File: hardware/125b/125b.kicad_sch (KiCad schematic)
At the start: 49 parts, among them J1 Guitar in, J2 Barrel_Jack, J3 Conn_02x05_Odd_Even_MountingP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, J4 Guitar out, SW1 SW_DIP_x02, SW2 RotaryEncoder_Switch, SW3 Switch 1, SW4 Switch 2, U1 L78L05_TO92, U2 TL074

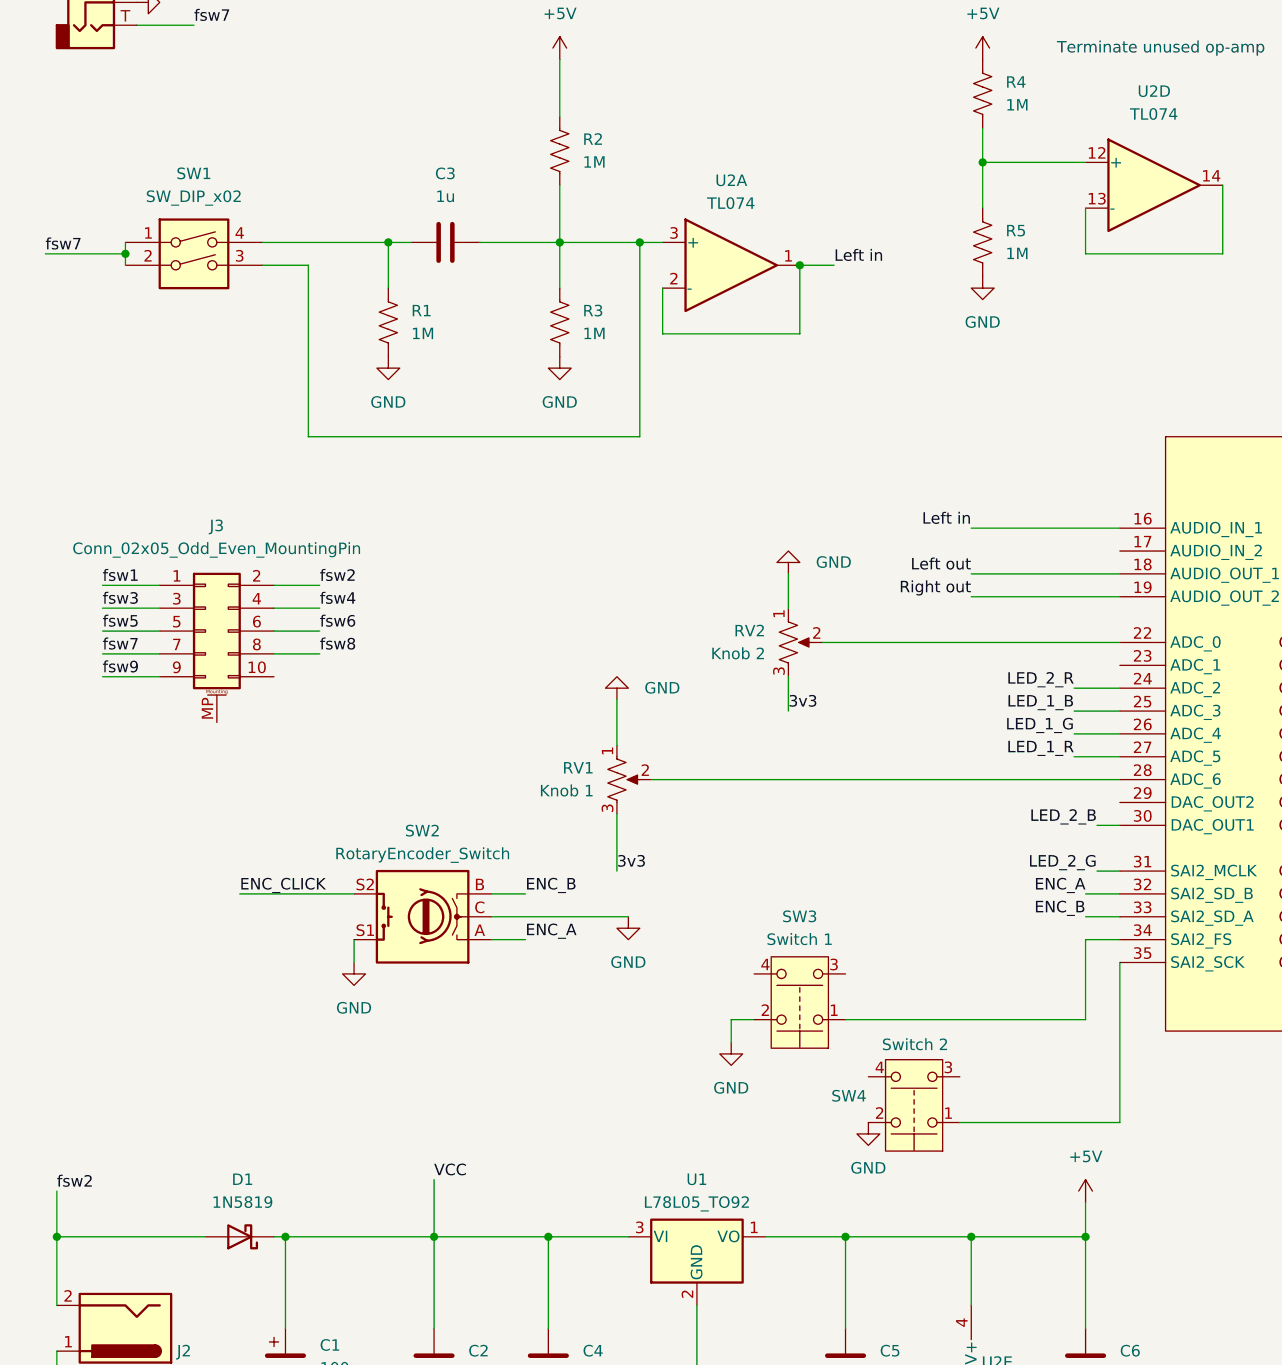
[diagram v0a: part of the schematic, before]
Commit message: Send switches to IDC; spdt for line level
Also fix line level to go straight to left in
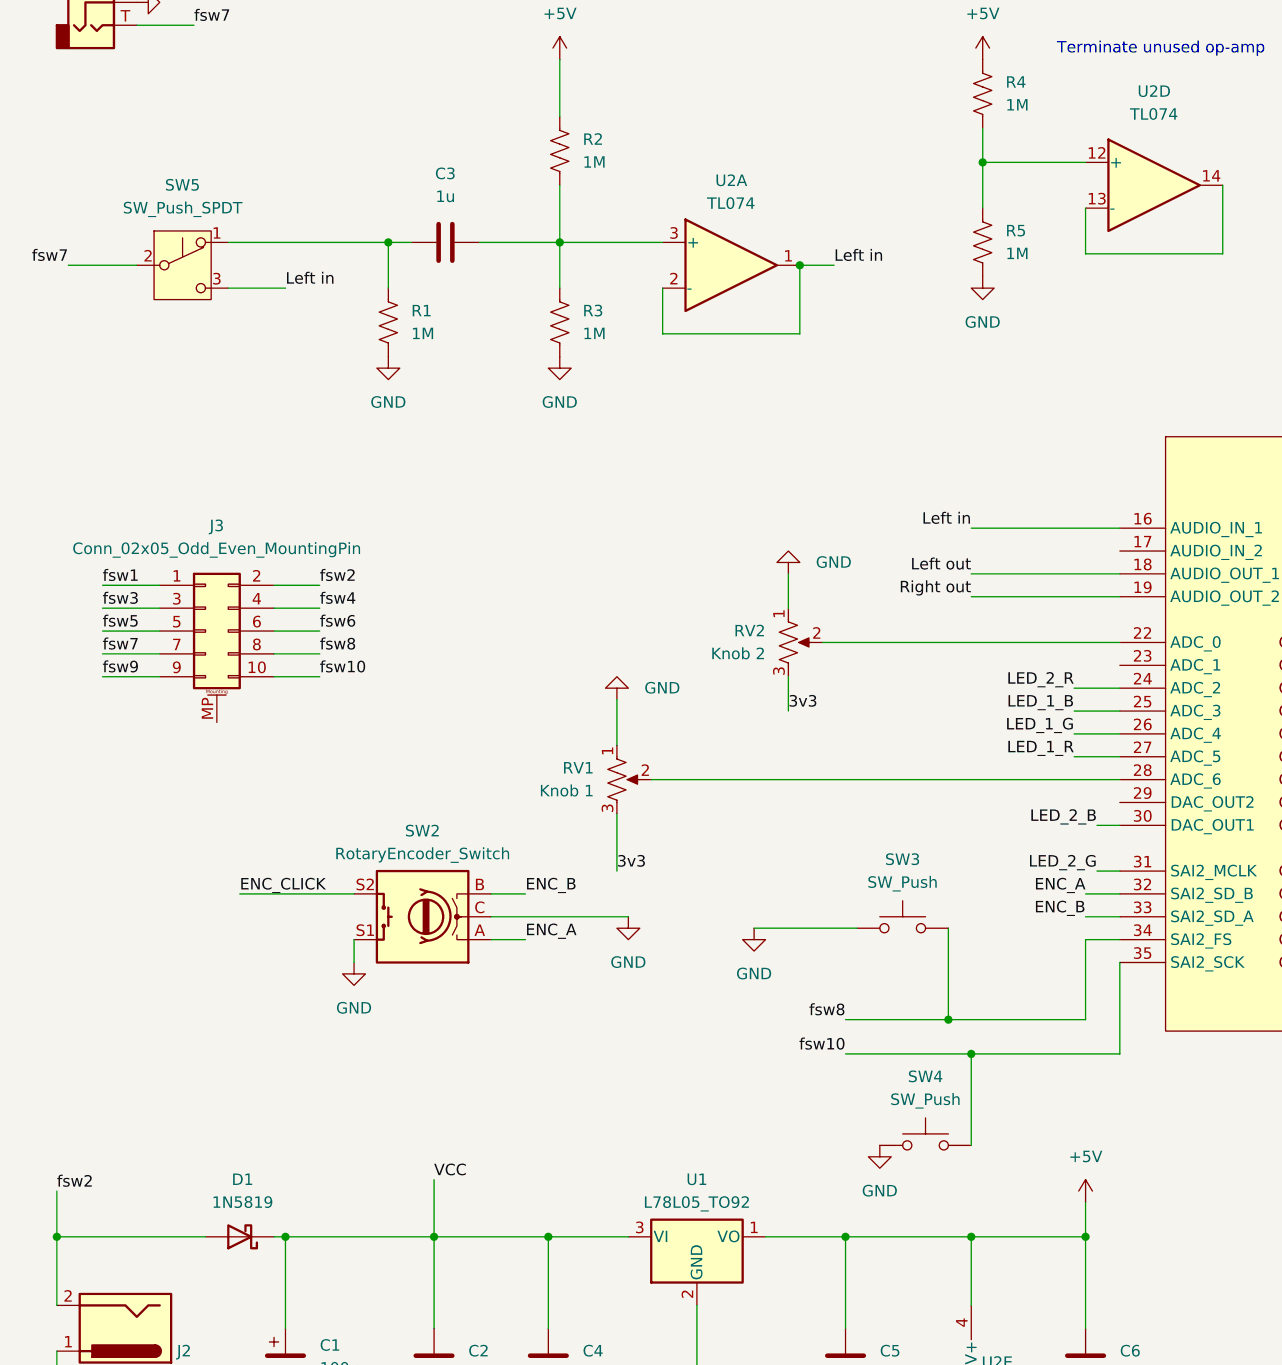
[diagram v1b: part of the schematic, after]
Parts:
- removed SW1: SW_DIP_x02, Button_Switch_THT:SW_DIP_SPSTx02_Slide_9.78x7.26mm_W7.62mm_P2.54mm, symbol Switch:SW_DIP_x02
- removed SW3: Switch 1, Connector_Wire:SolderWire-0.5sqmm_1x02_P4.6mm_D0.9mm_OD2.1mm, symbol Switch:SW_Push_Dual
- removed SW4: Switch 2, Connector_Wire:SolderWire-0.5sqmm_1x02_P4.6mm_D0.9mm_OD2.1mm, symbol Switch:SW_Push_Dual
- added SW3, SW4: SW_Push, symbol Switch:SW_Push
- added SW5: SW_Push_SPDT, symbol Switch:SW_Push_SPDT
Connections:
- net GND: now also SW3.1, SW4.1
- net Left in: now also SW5.3 (C)
- net fsw7: now also SW5.2 (B)
- net fsw8: now also A1.34 (SAI2_FS), SW3.2
- net fsw10: now reaches A1.35 (SAI2_SCK)
- net fsw10: now also J3.10 (Pin_10), SW4.2
- net at C3.1, R1.1: now also SW5.1 (A)

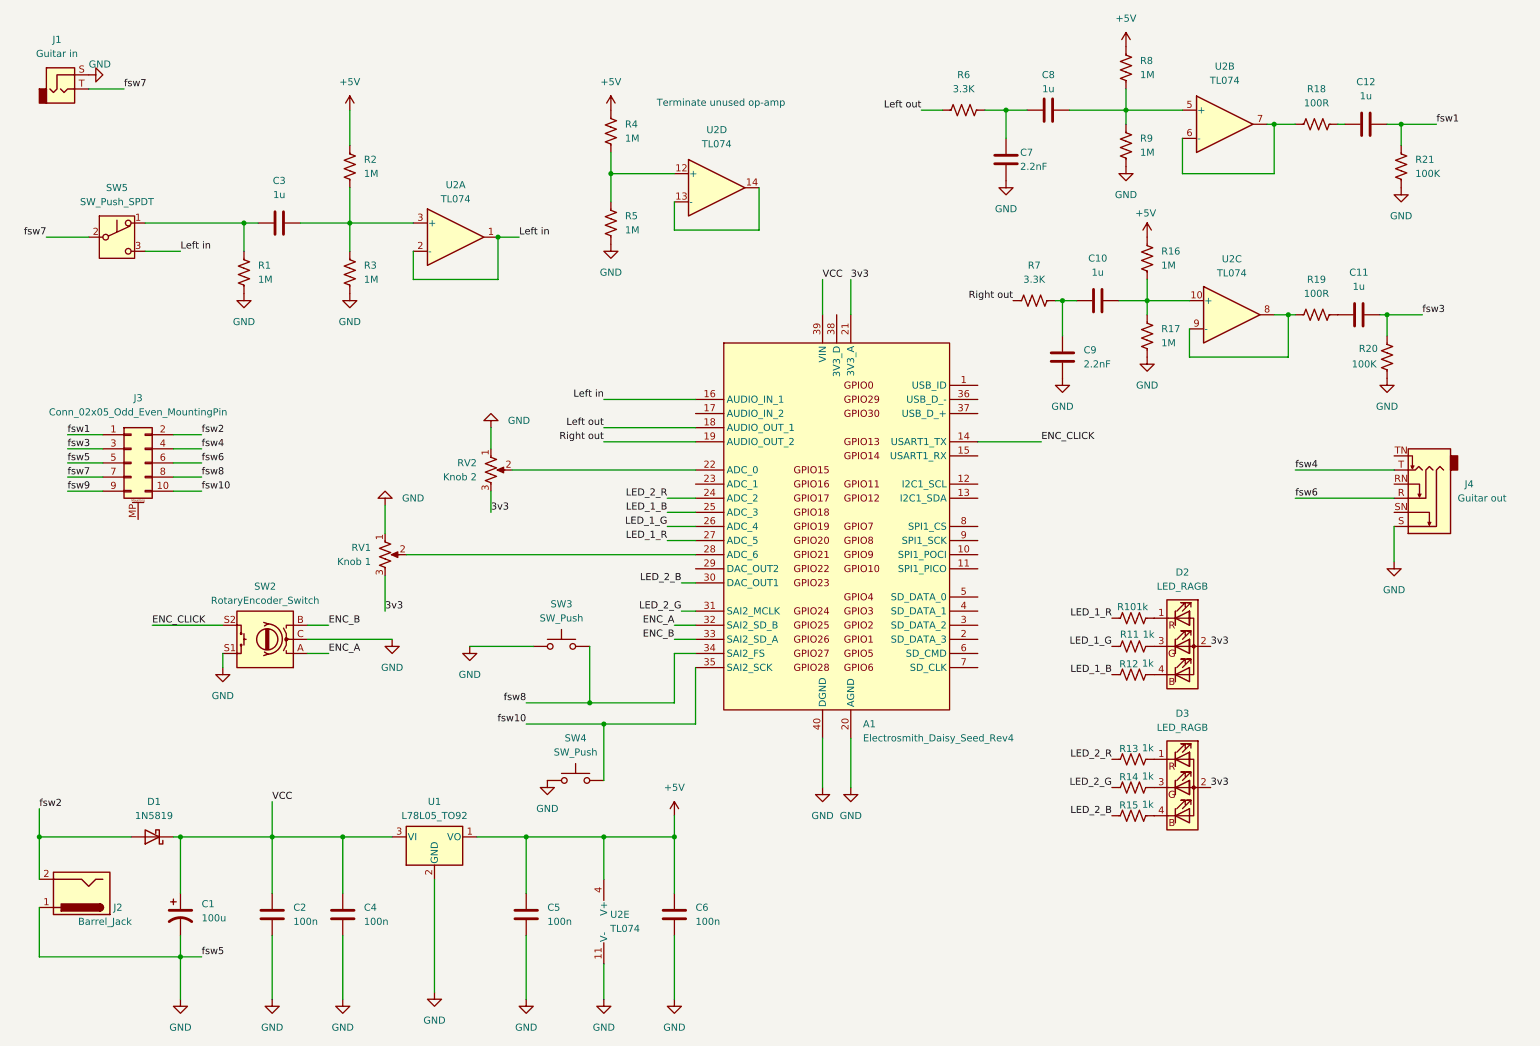
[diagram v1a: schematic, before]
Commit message: get new stereo sockets on schematic and pcb
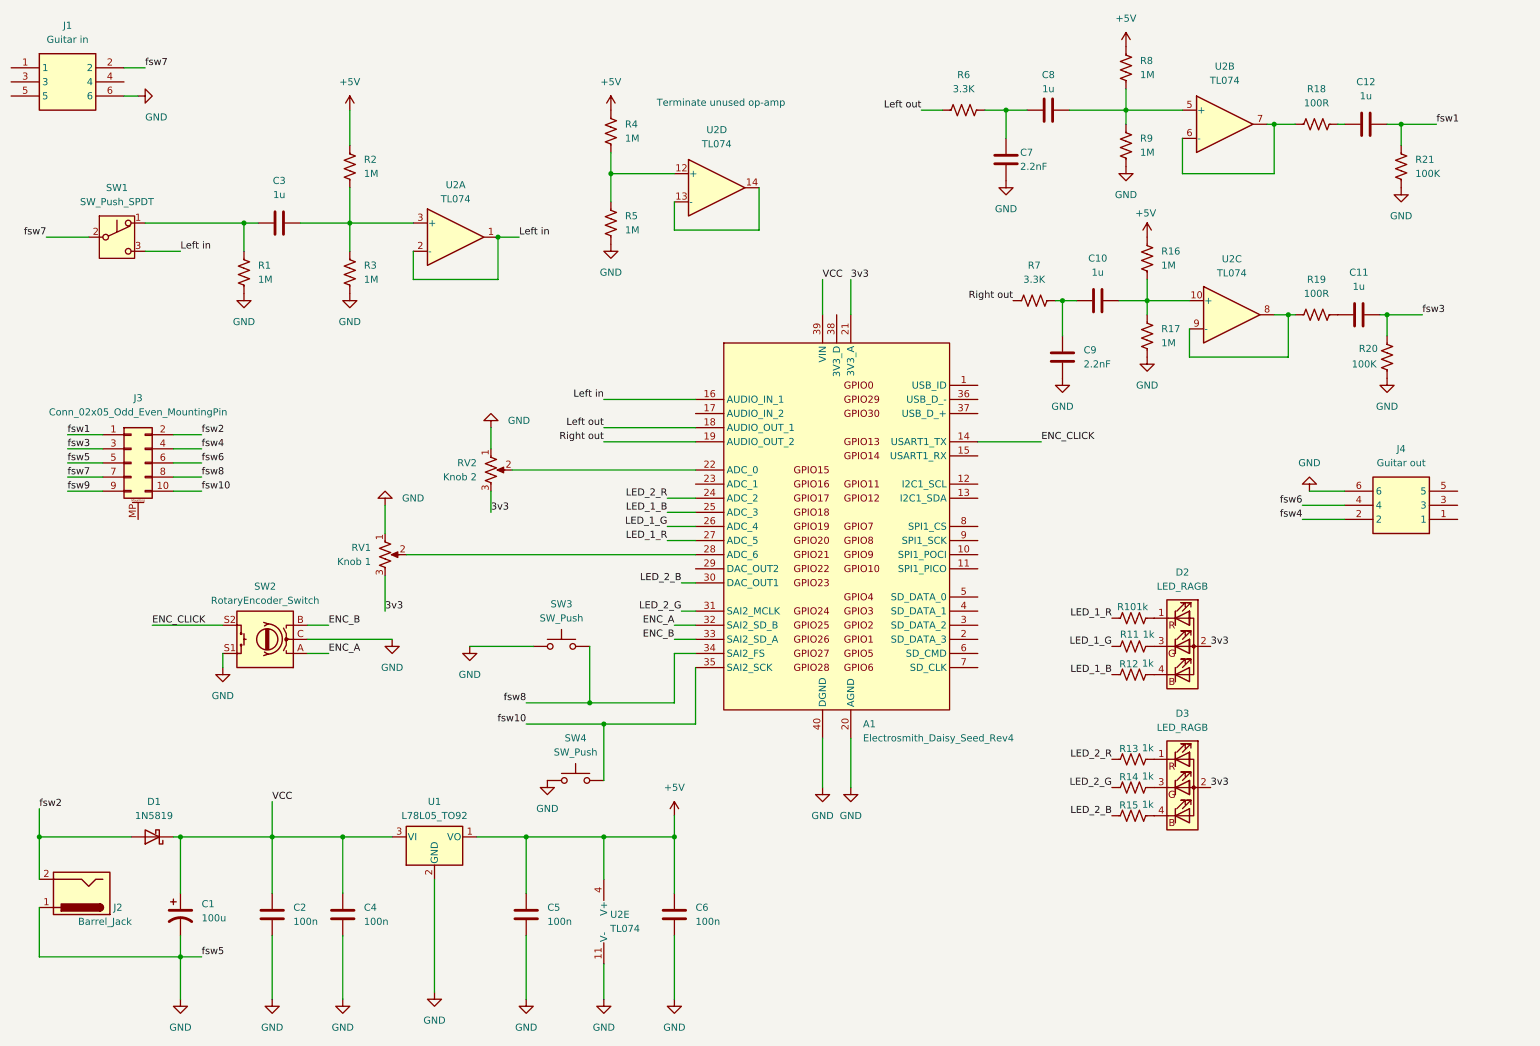
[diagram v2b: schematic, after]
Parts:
- removed J1: Guitar in, Project:Jack_6.35mm_Neutrik_NRJ6HF-1-AU_Horizontal, symbol Connector_Audio:AudioJack2
- removed J4: Guitar out, Project:Jack_6.35mm_Neutrik_NRJ6HF-1-AU_Horizontal, symbol Connector_Audio:NRJ6HF
- added J1: Guitar in, NYS215, symbol NYS215:NYS215
- added J4: Guitar out, NYS215, symbol NYS215:NYS215
- renumbered SW5 to SW1
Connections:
- net GND: now also J1.6, J4.6
- net fsw4: now also J4.2
- net fsw6: now also J4.4
- net fsw7: now also J1.2

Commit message: Wire connectors for push switches and add slide spdt
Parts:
- J1, J4: footprint NYS215 -> Project:NYS215
- SW1: footprint (none) -> PCM_4ms_Switch:Switch_Toggle_SPDT_SubMini
- SW3, SW4: footprint (none) -> Connector_Wire:SolderWire-0.5sqmm_1x02_P4.6mm_D0.9mm_OD2.1mm
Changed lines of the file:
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@@
 			)
 		)
-		(property "Footprint" ""
+		(property "Footprint" "Connector_Wire:SolderWire-0.5sqmm_1x02_P4.6mm_D0.9mm_OD2.1mm"
 			(at 115.57 146.05 0)
 			(effects
@@
 			)
 		)
-		(property "Footprint" ""
+		(property "Footprint" "Connector_Wire:SolderWire-0.5sqmm_1x02_P4.6mm_D0.9mm_OD2.1mm"
 			(at 113.03 121.92 0)
 			(effects
@@
 			)
 		)
-		(property "Footprint" "NYS215"
+		(property "Footprint" "Project:NYS215"
 			(at 257.81 9.22 0)
 			(effects
@@
 			)
 		)
-		(property "Footprint" "NYS215"
+		(property "Footprint" "Project:NYS215"
 			(at 30.48 117.78 0)
 			(effects
@@
 			)
 		)
-		(property "Footprint" ""
+		(property "Footprint" "PCM_4ms_Switch:Switch_Toggle_SPDT_SubMini"
 			(at 33.02 53.34 0)
 			(effects
